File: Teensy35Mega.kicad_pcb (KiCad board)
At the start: 2 copper layers, 68.6 x 114.3 mm, 34 parts, among them CON1 BARREL_JACK, J1 CONN_01X03, J2 CONN_01X02, P1 CONN_01X08, P10 CONN_02X18, P11 CONN_01X24, P12 CONN_01X08, P13 CONN_01X08, P14 CONN_01X08, P15 CONN_02X03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

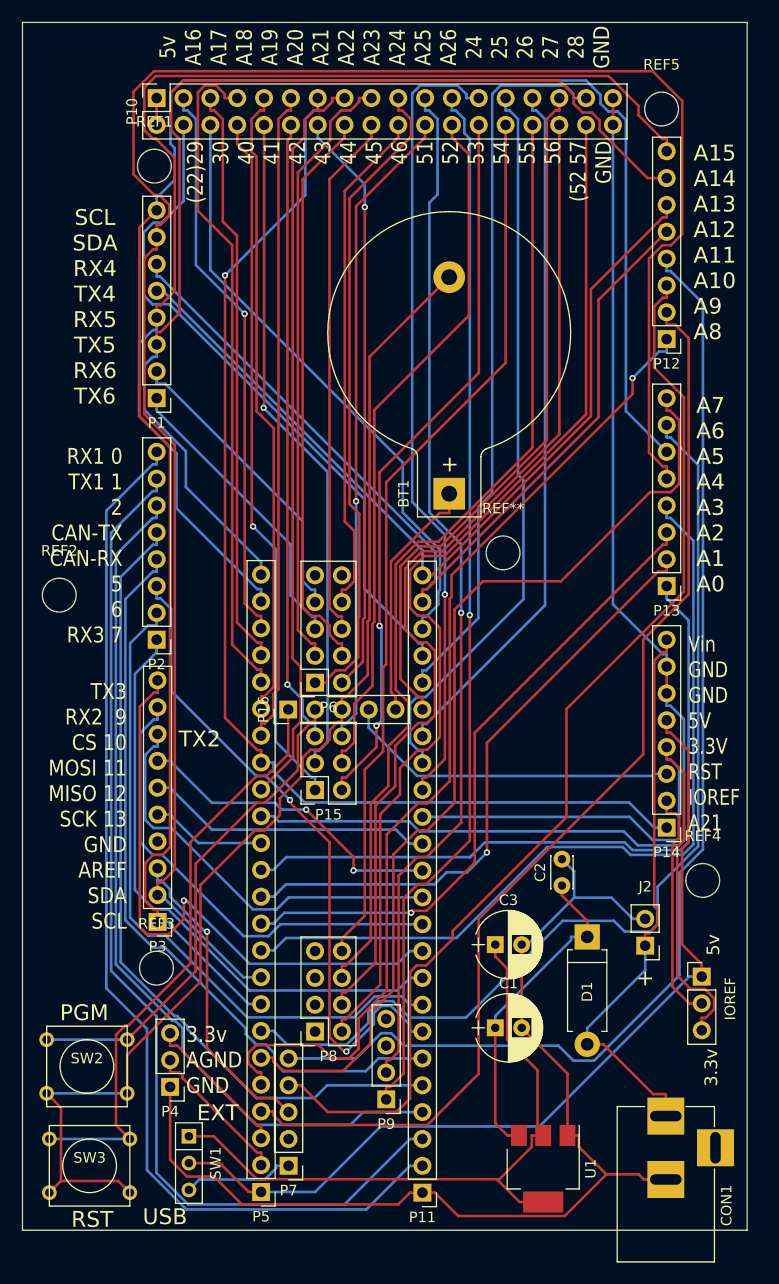
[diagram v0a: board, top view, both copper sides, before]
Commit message: Updated P8 connections & Layout
Updated P8 connections. per @boelle on PRJC Forum
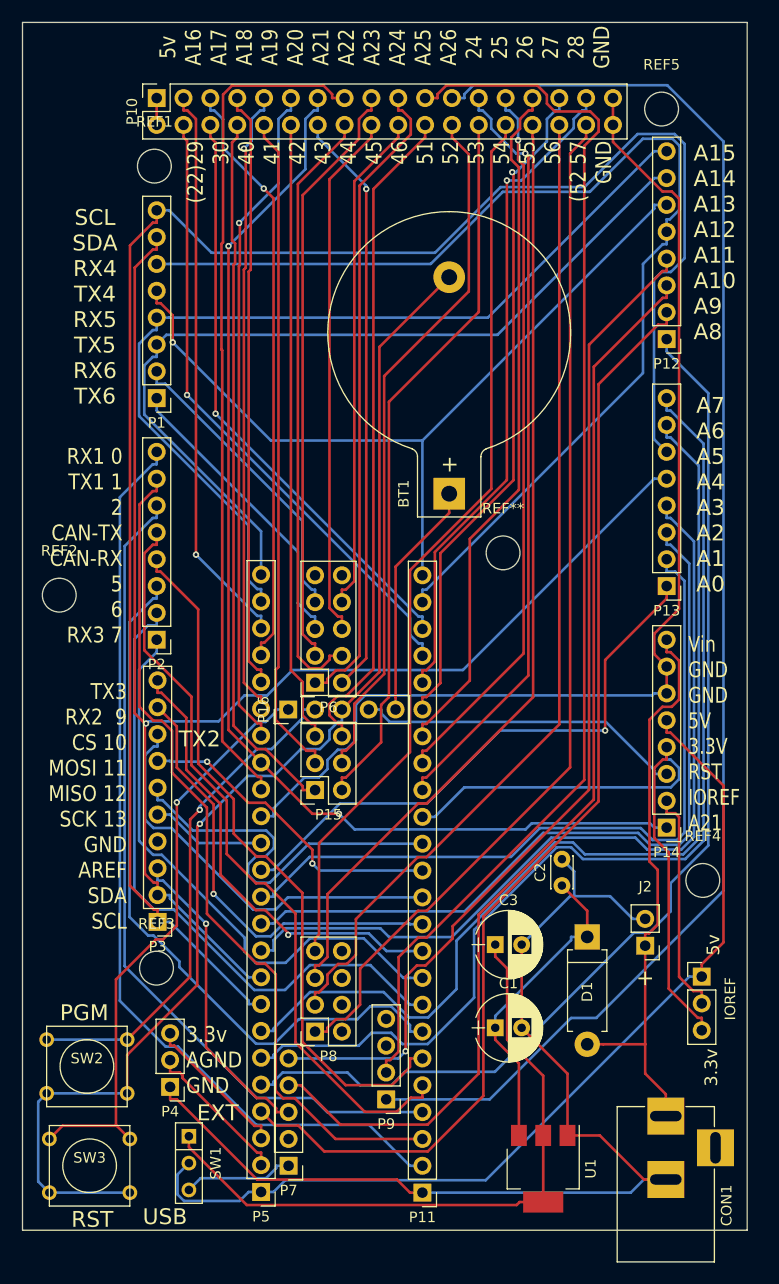
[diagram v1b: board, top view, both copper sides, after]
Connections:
- P8 pad 1: Net-(P8-Pad1) -> Net-(P10-Pad34)
- P8 pad 2: Net-(P10-Pad34) -> Net-(P8-Pad2)
- P8 pad 3: Net-(P8-Pad3) -> Net-(P10-Pad32)
- P8 pad 4: Net-(P10-Pad32) -> Net-(P8-Pad4)
- P8 pad 5: Net-(P8-Pad5) -> Net-(P10-Pad30)
- P8 pad 6: Net-(P10-Pad30) -> Net-(P8-Pad6)
- P8 pad 7: Net-(P8-Pad7) -> Net-(P10-Pad28)
- P8 pad 8: Net-(P10-Pad28) -> Net-(P8-Pad8)
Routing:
- net Net-(P1-Pad7): track 186.6 -> 136.6 mm, vias 0 -> 1
- net Net-(P10-Pad23): track 99.6 -> 139.6 mm, vias 1 -> 0
- net Net-(P1-Pad4): track 110.9 -> 87.5 mm
- net Net-(P1-Pad3): track 104.5 -> 81.8 mm
- net Net-(P10-Pad21): track 98.2 -> 118.1 mm, vias 1 -> 0
- net Net-(P1-Pad6): track 88.6 -> 108.5 mm
- net Net-(P11-Pad3): track 98.4 -> 80.9 mm
- net Net-(P12-Pad4): track 112.8 -> 97.3 mm, vias 0 -> 1
- net Net-(P11-Pad10): track 56.6 -> 43.4 mm
- net Net-(P13-Pad1): track 67.3 -> 54.1 mm, vias 0 -> 1
- net Net-(P13-Pad3): track 61.6 -> 74.7 mm, vias 1 -> 0
- net Net-(P13-Pad2): track 58.4 -> 70.8 mm, vias 1 -> 0
- net Net-(P11-Pad2): track 101.1 -> 88.7 mm
- net Net-(P11-Pad14): track 27.3 -> 37.0 mm
- net Net-(P10-Pad15): track 70.5 -> 80.1 mm
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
